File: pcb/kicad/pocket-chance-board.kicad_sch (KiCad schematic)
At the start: 123 parts, among them J1 SWD, J2 USB4085-GF-A, J3 LiPo JST-PH 2.0mm (pin 1 = + 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, J4 LCD 1.54in ST7789 module, JST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, J5 Speaker JST-PH, J6 microSD Molex 104031-0811, J7 STEMMA QT, J8 Expansion, Q1 FS8205A, Q2 DMG2305UX, SW1 BOOT, SW10 JOY LEFT, SW11 JOY RIGHT, SW12 JOY PRESS, SW2 RESET, SW3 POWER PCM12, SW4 A PTS125SM43SMTR2LFS, SW5 B PTS125SM43SMTR2LFS, SW6 X PTS125SM43SMTR2LFS, SW7 Y PTS125SM43SMTR2LFS, SW8 JOY UP, SW9 JOY DOWN, U1 RP2350A, U10 LSM6DSOXTR, U11 RM2, U2 W25Q128JVSIQ, U3 APS6404L-3SQR-SN, U4 USBLC6-2SC6, U5 BQ24074RGTR, U6 TPS63001DRCR, U7 DW01A, U8 PAM8302AADCR, U9 DS3231MZ+, Y1 12MHz ABM8-272-T3

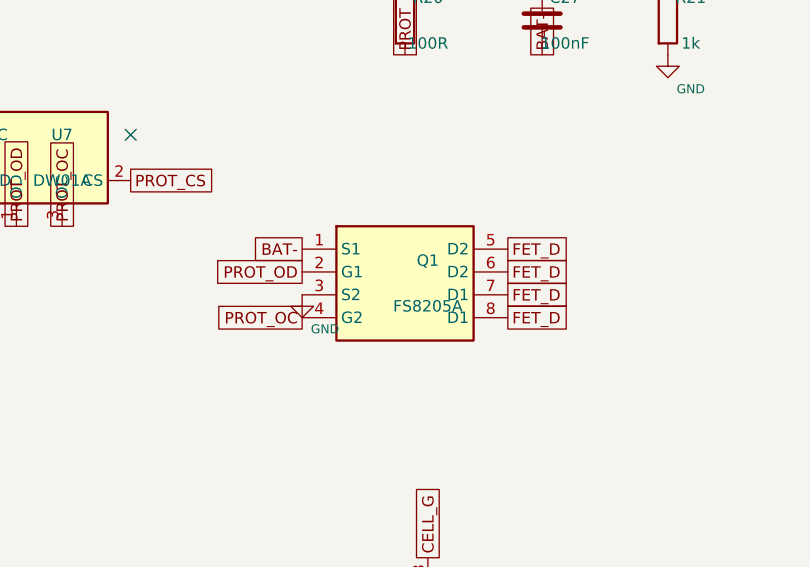
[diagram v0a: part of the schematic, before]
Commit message: FS8205A pin map from the datasheet; IMU on KiCad's ST LGA-14 footprint
Co-Authored-By: Claude Fable 5.1 <noreply@anthropic.com>
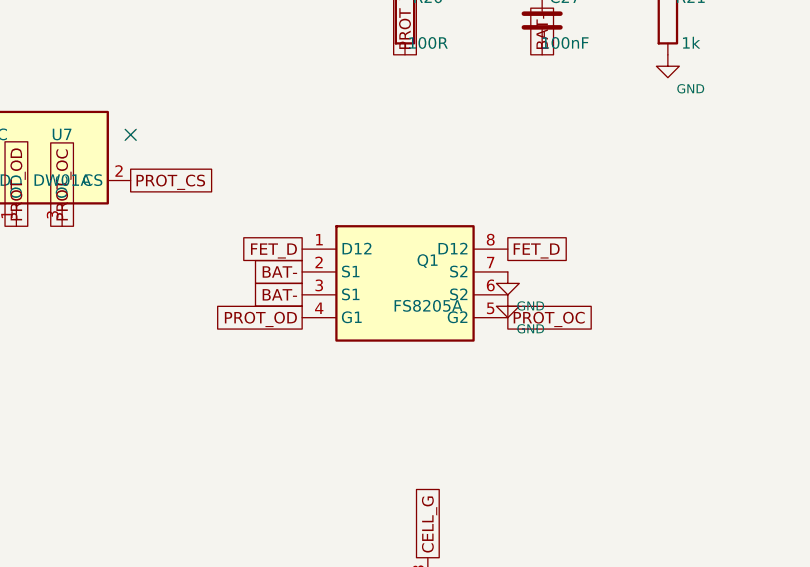
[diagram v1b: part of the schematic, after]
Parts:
- U10: footprint pcb_custom:ST_LGA-14_2.5x3mm -> Package_LGA:LGA-14_3x2.5mm_P0.5mm_LayoutBorder3x4y
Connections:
- net BAT-: now also Q1.2 (S1), Q1.3 (S1); no longer Q1.1 (S1)
- net FET_D: now also Q1.1 (D12); no longer Q1.5 (D2), Q1.6 (D2), Q1.7 (D1)
- net GND: now also Q1.6 (S2), Q1.7 (S2); no longer Q1.3 (S2)
- net PROT_OC: now also Q1.5 (G2); no longer Q1.4 (G2)
- net PROT_OD: now also Q1.4 (G1); no longer Q1.2 (G1)
